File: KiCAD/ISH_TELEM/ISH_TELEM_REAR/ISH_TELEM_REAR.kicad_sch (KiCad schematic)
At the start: 37 parts, among them Q1 AO3400, Q2 AO3401A, U1 ADS1115IDGS, U2 MCP1703Ax-400xxTT, U3 MCP1703Ax-400xxTT, U4 MCP6002-xP, U5 ADS1115IDGS

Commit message: Changed some V step up stuff
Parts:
- removed C3, C4: 1uf, symbol Device:C
- removed D1: D_Schottky, symbol Device:D_Schottky
- removed R11: 10K, symbol Device:R
- removed R12: 1K, symbol Device:R
- removed R13: 1K?, symbol Device:R
- removed U3: MCP1703Ax-400xxTT, Package_TO_SOT_SMD:SOT-23, symbol Regulator_Linear:MCP1703Ax-400xxTT
- R10: value 10K -> 1K
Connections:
- net GND: no longer Q1.3 (D), R10.2
- net MC In: now also Q1.3 (D), R10.2; no longer C7.1, R10.1, U2.2 (VO)
- net Motor PWM Driver: no longer Q2.1 (G)
- net Throttle Pot / Hall effect: now reaches U5.7 (AIN3)
- new net: C7.1, R10.1, U2.2 (VO)
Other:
- note added: "4v regulator (Might change to 5v because of ease of acces. Just needs some software adjustments.)"
- note added: "PWM step up from 3.3v to 4v. This works on PROTO."
- note removed: "Or diode here. Not really sure about this section, best to just experiment when we work on a breadboard I think."
- note removed: "PWM step up from 3.3v to 4v"
- note removed: "PWM step up from 3.3v to 4v (Alternative)"
- moved on the sheet: R10

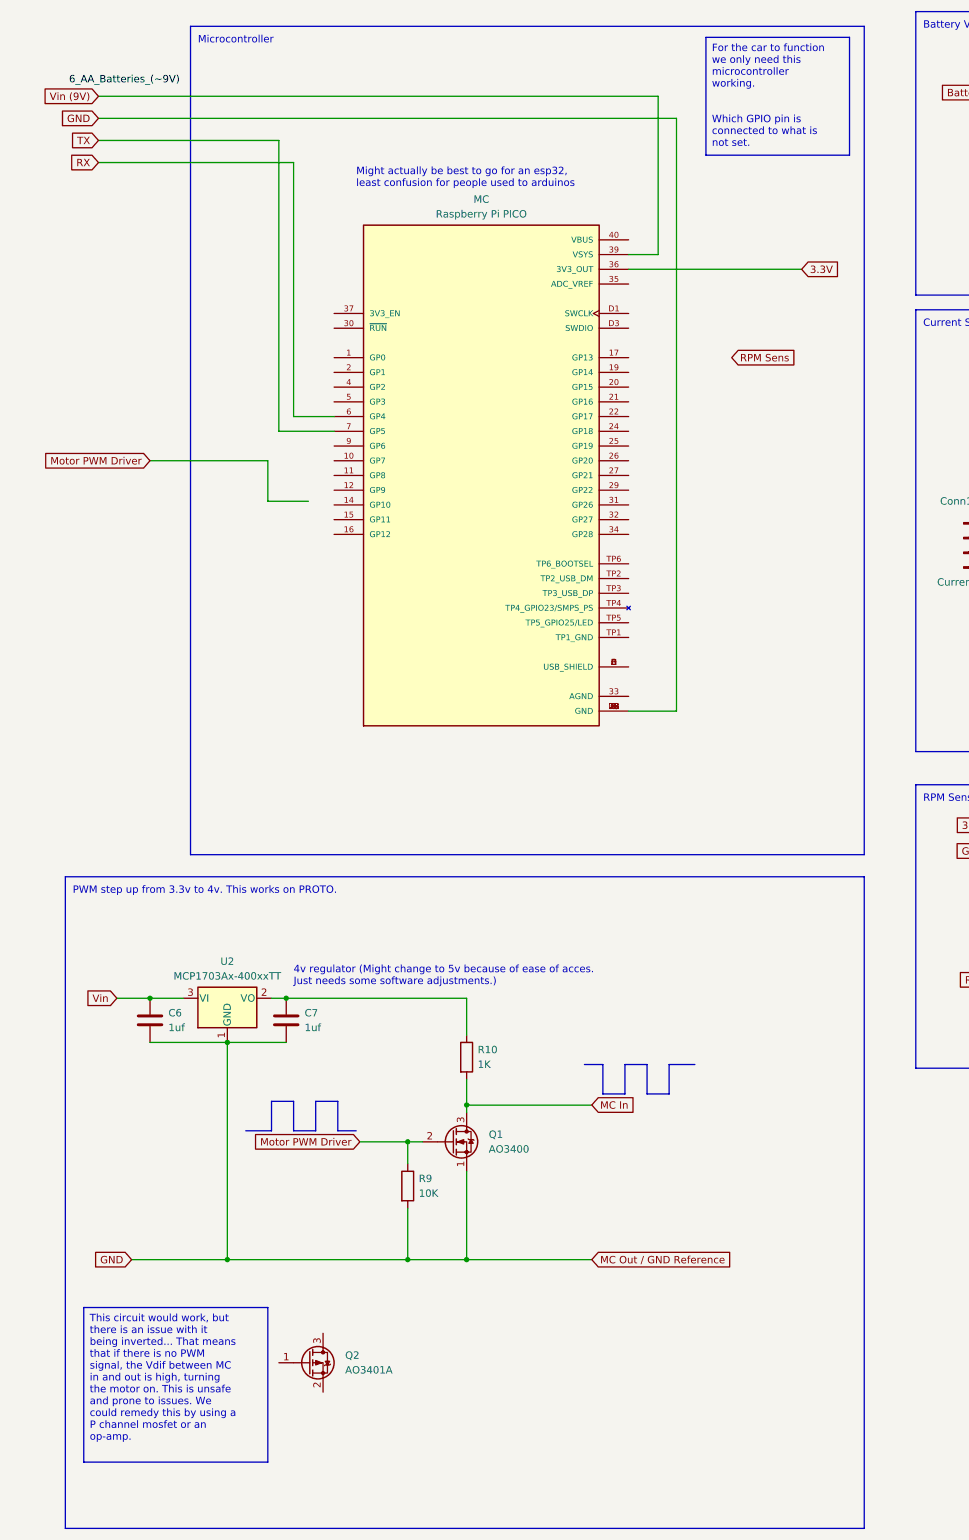
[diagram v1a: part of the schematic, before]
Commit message: Updated the KICAD schematic
Added the working PWM amplifier and replaced the Microcontroller with ESP32
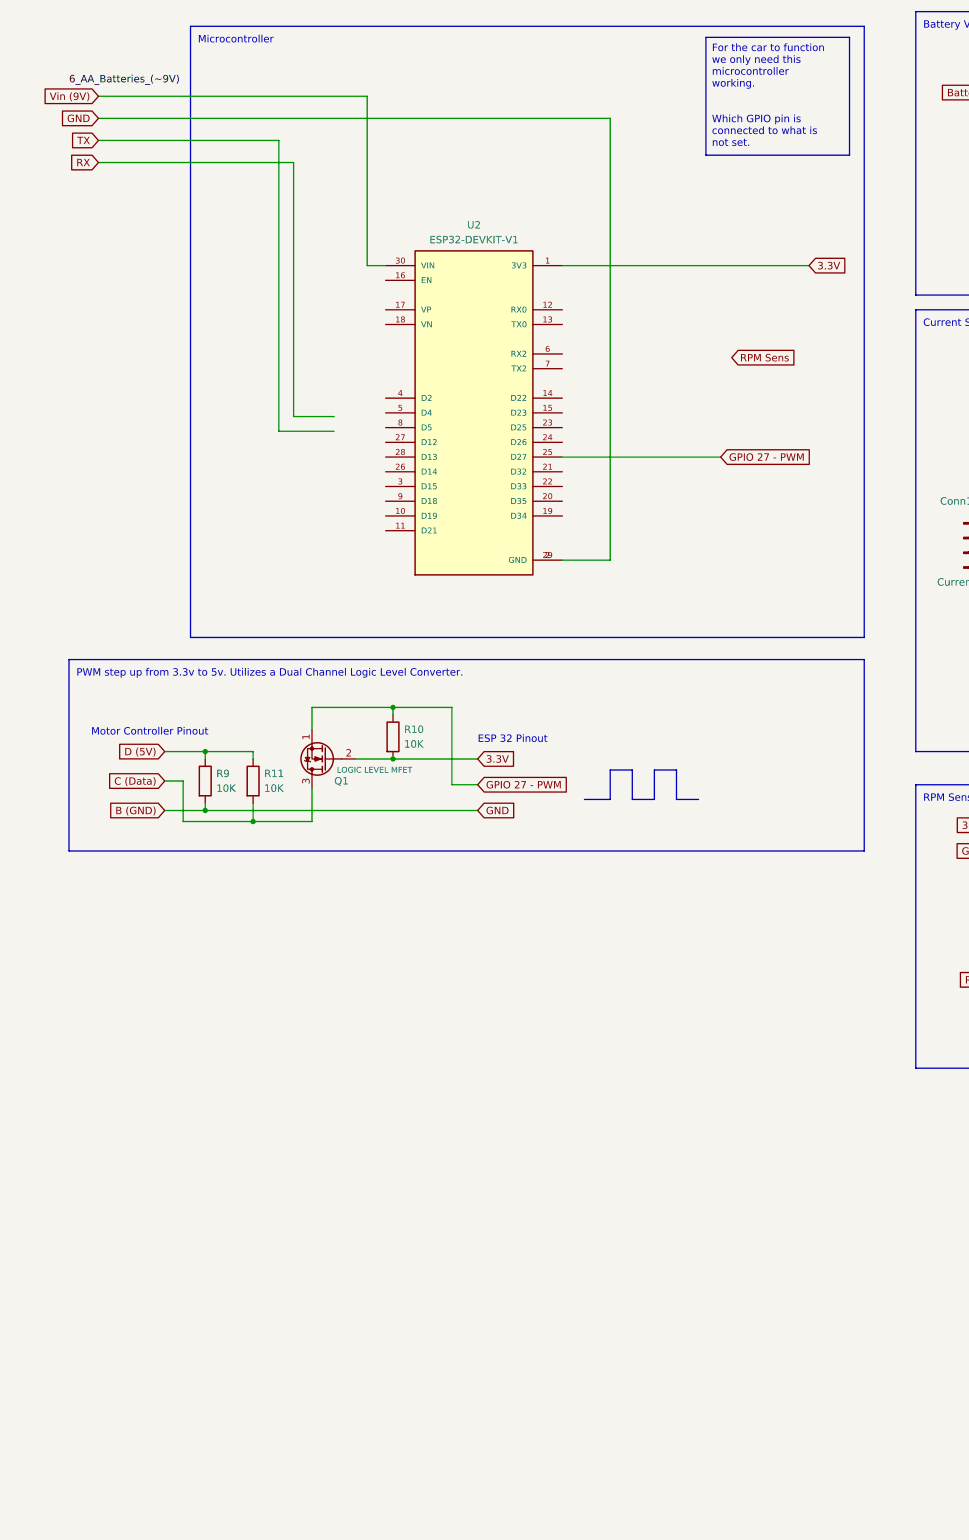
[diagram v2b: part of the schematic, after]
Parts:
- removed C6, C7: 1uf, symbol Device:C
- removed MC: Raspberry Pi PICO, SC0915:MODULE_SC0915, symbol SC0915:SC0915
- removed Q2: AO3401A, Package_TO_SOT_SMD:SOT-23, symbol Transistor_FET:AO3401A
- removed U2: MCP1703Ax-400xxTT, Package_TO_SOT_SMD:SOT-23, symbol Regulator_Linear:MCP1703Ax-400xxTT
- added R11: 10K, symbol Device:R
- added U2: ESP32-DEVKIT-V1, ESP32-DEVKIT-V1:MODULE_ESP32_DEVKIT_V1, symbol ESP32-DEVKIT-V1:ESP32-DEVKIT-V1
- Q1: value AO3400 -> LOGIC LEVEL MFET; footprint Package_TO_SOT_THT:TO-92_Inline -> (none)
- R10: value 1K -> 10K
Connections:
- net 3.3V: now also Q1.2 (G), R10.2, U2.1 (3V3)
- net GND: now also U2.2 (GND), U2.29 (GND); no longer Q1.1 (S)
- net Vin (9V): now also U2.30 (VIN)
- net GPIO 27 - PWM: now reaches R10.1
- net GPIO 27 - PWM: now also Q1.1 (S), U2.25 (D27)
- net MC In renamed C (Data)
- net C (Data): now also R11.2; no longer R10.2
- net Motor PWM Driver renamed D (5V)
- net D (5V): now also R11.1; no longer Q1.2 (G)
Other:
- note added: "ESP 32 Pinout"
- note added: "Motor Controller Pinout"
- note added: "PWM step up from 3.3v to 5v. Utilizes a Dual Channel Logic Level Converter."
- note removed: "4v regulator (Might change to 5v because of ease of acces. Just needs some software adjustments.)"
- note removed: "Might actually be best to go for an esp32, least confusion for people used to arduinos"
- note removed: "PWM step up from 3.3v to 4v. This works on PROTO."
- moved on the sheet: Q1, R10, R9
